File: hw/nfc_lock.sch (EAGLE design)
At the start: 27 parts, among them IC1 STM8S003F3, IC3 MCP170312MB, Q1 8MHz, U1 M24SR16-YMN6T/2, U2 IRFML8244TRPBF, U3 IRFML8244TRPBF, U4 2N7002BKW, X1 MINI-USB-32005-301

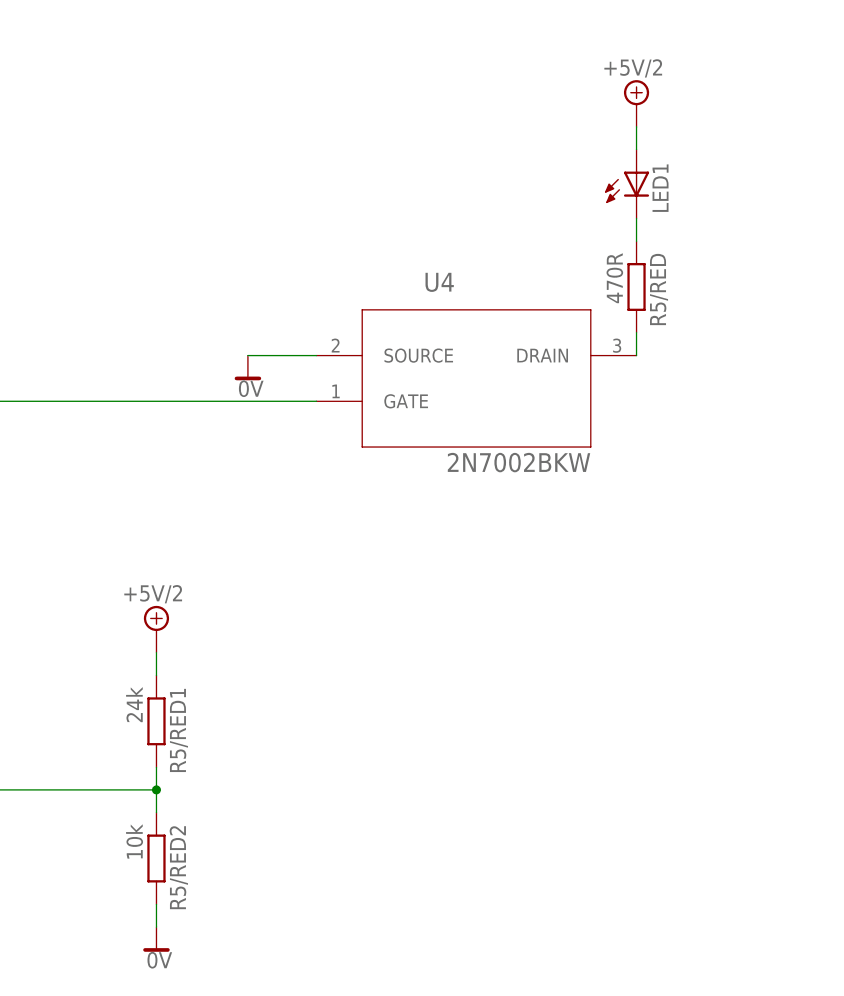
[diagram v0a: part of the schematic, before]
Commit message: resistors not LEDs for voltage split
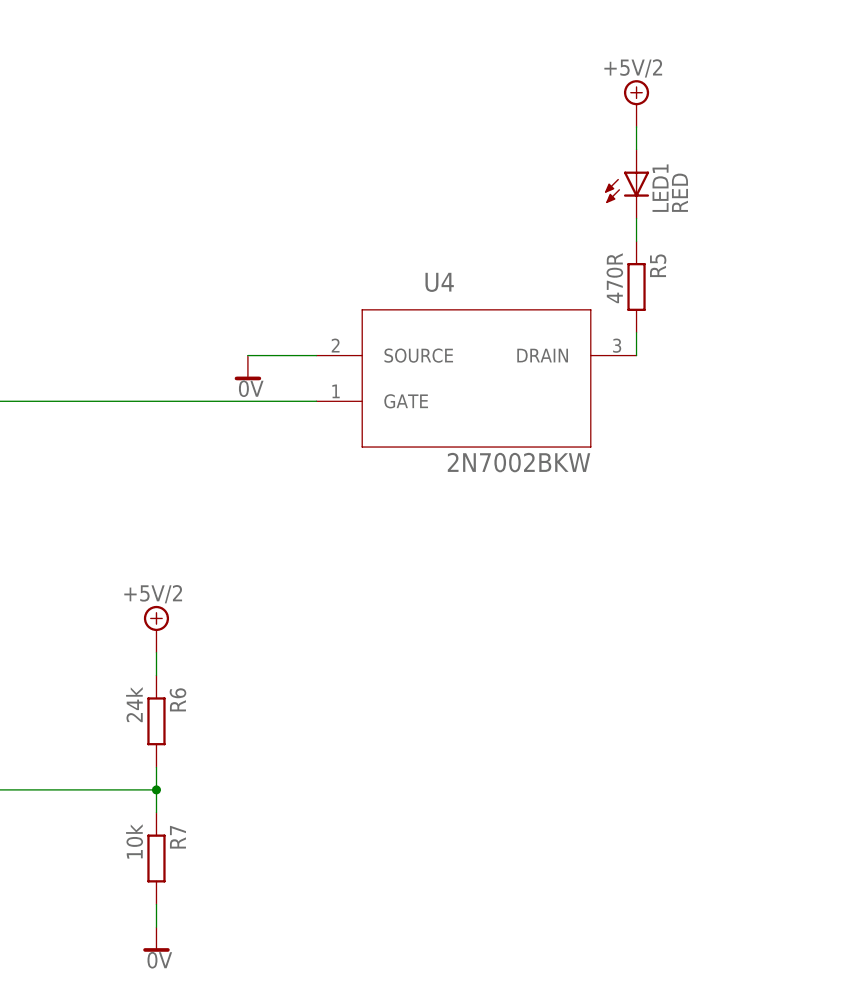
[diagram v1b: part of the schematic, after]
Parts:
- LED1: value (none) -> RED
- renumbered R5/RED to R5, R5/RED1 to R6, R5/RED2 to R7
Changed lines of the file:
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@@
 <part name="SUPPLY25" library="supply2" deviceset="+5V/1" device="" value="+3.3V"/>
 <part name="U4" library="2n7002" deviceset="2N7002BKW" device=""/>
-<part name="LED1" library="led" deviceset="LED" device="CHIP-LED0603"/>
-<part name="R5/RED" library="rcl" deviceset="R-EU_" device="R0805" value="470R"/>
+<part name="LED1" library="led" deviceset="LED" device="CHIP-LED0603" value="RED"/>
+<part name="R5" library="rcl" deviceset="R-EU_" device="R0805" value="470R"/>
 <part name="SUPPLY26" library="supply2" deviceset="0V" device=""/>
 <part name="C4" library="rcl" deviceset="CPOL-EU" device="153CLV-0405" value="1uF"/>
@@
 <part name="SUPPLY28" library="supply2" deviceset="0V" device=""/>
 <part name="SUPPLY29" library="supply2" deviceset="0V" device=""/>
-<part name="R5/RED1" library="rcl" deviceset="R-EU_" device="R0805" value="24k"/>
-<part name="R5/RED2" library="rcl" deviceset="R-EU_" device="R0805" value="10k"/>
+<part name="R6" library="rcl" deviceset="R-EU_" device="R0805" value="24k"/>
+<part name="R7" library="rcl" deviceset="R-EU_" device="R0805" value="10k"/>
 <part name="SUPPLY30" library="supply2" deviceset="0V" device=""/>
 <part name="SUPPLY31" library="supply2" deviceset="+5V/2" device=""/>
@@
 <instance part="U4" gate="A" x="116.84" y="0"/>
 <instance part="LED1" gate="G$1" x="152.4" y="20.32"/>
-<instance part="R5/RED" gate="G$1" x="152.4" y="7.62" rot="R270"/>
+<instance part="R5" gate="G$1" x="152.4" y="7.62" rot="R270"/>
 <instance part="SUPPLY26" gate="0V" x="109.22" y="-2.54"/>
 <instance part="C4" gate="G$1" x="-15.24" y="81.28"/>
@@
 <instance part="SUPPLY28" gate="0V" x="-33.02" y="60.96"/>
 <instance part="SUPPLY29" gate="0V" x="-33.02" y="53.34"/>
-<instance part="R5/RED1" gate="G$1" x="99.06" y="-40.64" rot="R270"/>
-<instance part="R5/RED2" gate="G$1" x="99.06" y="-55.88" rot="R270"/>
+<instance part="R6" gate="G$1" x="99.06" y="-40.64" rot="R270"/>
+<instance part="R7" gate="G$1" x="99.06" y="-55.88" rot="R270"/>
 <instance part="SUPPLY30" gate="0V" x="99.06" y="-66.04"/>
 <instance part="SUPPLY31" gate="G$1" x="-63.5" y="111.76"/>
@@
 </segment>
 <segment>
-<pinref part="R5/RED2" gate="G$1" pin="2"/>
+<pinref part="R7" gate="G$1" pin="2"/>
 <pinref part="SUPPLY30" gate="0V" pin="0V"/>
 <wire x1="99.06" y1="-63.5" x2="99.06" y2="-60.96" width="0.1524" layer="91"/>
@@
 </segment>
 <segment>
-<pinref part="R5/RED1" gate="G$1" pin="1"/>
+<pinref part="R6" gate="G$1" pin="1"/>
 <pinref part="SUPPLY32" gate="G$1" pin="+5V/2"/>
 <wire x1="99.06" y1="-33.02" x2="99.06" y2="-35.56" width="0.1524" layer="91"/>
@@
 <segment>
 <pinref part="LED1" gate="G$1" pin="C"/>
-<pinref part="R5/RED" gate="G$1" pin="1"/>
+<pinref part="R5" gate="G$1" pin="1"/>
 <wire x1="152.4" y1="15.24" x2="152.4" y2="12.7" width="0.1524" layer="91"/>
 </segment>
@@
 <net name="N$14" class="0">
 <segment>
-<pinref part="R5/RED" gate="G$1" pin="2"/>
+<pinref part="R5" gate="G$1" pin="2"/>
 <pinref part="U4" gate="A" pin="DRAIN"/>
 <wire x1="152.4" y1="0" x2="152.4" y2="2.54" width="0.1524" layer="91"/>
@@
 <wire x1="63.5" y1="66.04" x2="63.5" y2="-48.26" width="0.1524" layer="91"/>
 <wire x1="63.5" y1="-48.26" x2="99.06" y2="-48.26" width="0.1524" layer="91"/>
-<pinref part="R5/RED1" gate="G$1" pin="2"/>
-<pinref part="R5/RED2" gate="G$1" pin="1"/>
+<pinref part="R6" gate="G$1" pin="2"/>
+<pinref part="R7" gate="G$1" pin="1"/>
 <wire x1="99.06" y1="-50.8" x2="99.06" y2="-48.26" width="0.1524" layer="91"/>
 <wire x1="99.06" y1="-48.26" x2="99.06" y2="-45.72" width="0.1524" layer="91"/>

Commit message: antenna drawed
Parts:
- added R8: 30k, rcl:R-EU_R0805
- R4: value 10k -> 20k
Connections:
- net +5V/1: now also R8.2
- net N$7: now also R8.1
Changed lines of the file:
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@@
 <part name="SUPPLY23" library="supply2" deviceset="0V" device=""/>
 <part name="SUPPLY24" library="supply2" deviceset="0V" device=""/>
-<part name="R4" library="rcl" deviceset="R-EU_" device="R0805" value="10k"/>
+<part name="R4" library="rcl" deviceset="R-EU_" device="R0805" value="20k"/>
 <part name="SUPPLY25" library="supply2" deviceset="+5V/1" device="" value="+3.3V"/>
 <part name="U4" library="2n7002" deviceset="2N7002BKW" device=""/>
@@
 <part name="SUPPLY22" library="supply2" deviceset="+5V/2" device=""/>
 <part name="SUPPLY32" library="supply2" deviceset="+5V/2" device=""/>
+<part name="R8" library="rcl" deviceset="R-EU_" device="R0805" value="30k"/>
+<part name="SUPPLY33" library="supply2" deviceset="+5V/1" device="" value="+3.3V"/>
 </parts>
 <sheets>
@@
 <instance part="SUPPLY22" gate="G$1" x="152.4" y="27.94"/>
 <instance part="SUPPLY32" gate="G$1" x="99.06" y="-30.48"/>
+<instance part="R8" gate="G$1" x="96.52" y="99.06" rot="R90"/>
+<instance part="SUPPLY33" gate="G$1" x="96.52" y="109.22"/>
 </instances>
 <busses>
@@
 <pinref part="SUPPLY25" gate="G$1" pin="+5V/1"/>
 <wire x1="167.64" y1="99.06" x2="167.64" y2="96.52" width="0.1524" layer="91"/>
+</segment>
+<segment>
+<pinref part="R8" gate="G$1" pin="2"/>
+<pinref part="SUPPLY33" gate="G$1" pin="+5V/1"/>
+<wire x1="96.52" y1="106.68" x2="96.52" y2="104.14" width="0.1524" layer="91"/>
 </segment>
 </net>
@@
 <pinref part="U1" gate="G$1" pin="RFDISABLE"/>
 <wire x1="96.52" y1="81.28" x2="111.76" y2="81.28" width="0.1524" layer="91"/>
-</segment>
-</net>
+<pinref part="R8" gate="G$1" pin="1"/>
+<junction x="96.52" y="93.98"/>
+</segment>
+</net>

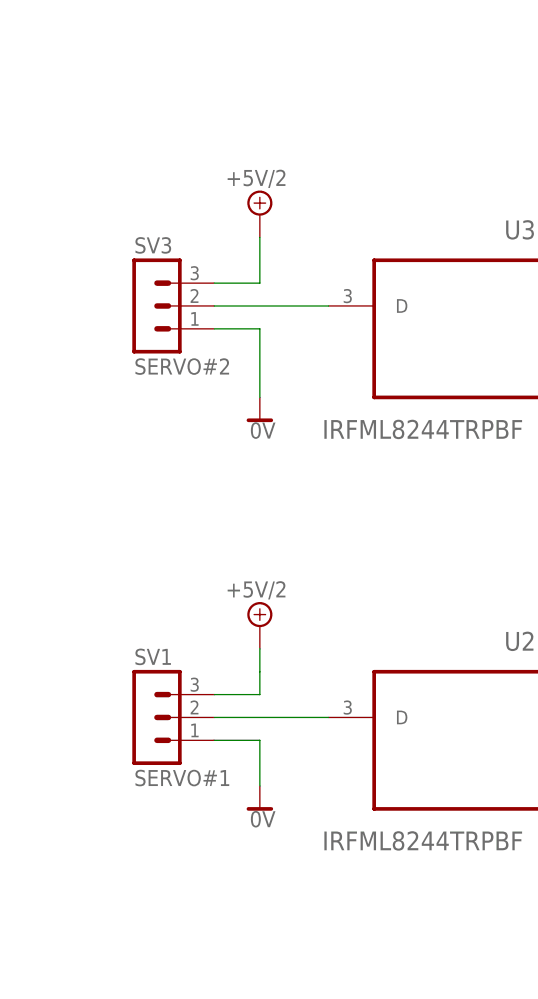
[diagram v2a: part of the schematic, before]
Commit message: added 2x more servos + some elements positioning
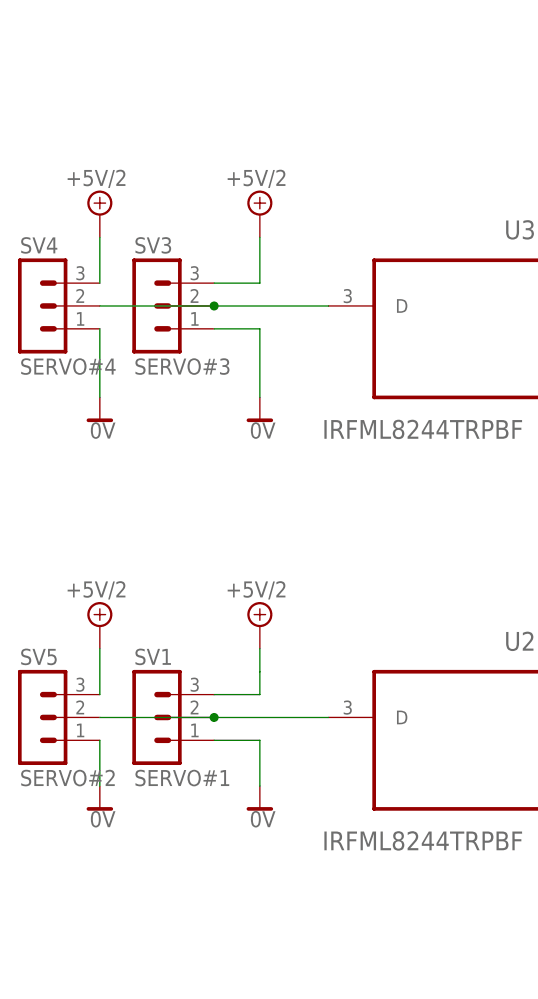
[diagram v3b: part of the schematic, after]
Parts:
- added SV4: SERVO#4, con-lstb:MA03-1
- added SV5: SERVO#2, con-lstb:MA03-1
- SV3: value SERVO#2 -> SERVO#3
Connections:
- net +5V/2: now also SV4.3, SV5.3
- net 0V: now also SV4.1, SV5.1
- net N$11: now also SV4.2
- net N$9: now also SV5.2
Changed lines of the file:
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@@
 <part name="SV2" library="con-lstb" deviceset="MA04-1" device="" value="SWIM"/>
 <part name="SUPPLY21" library="supply2" deviceset="0V" device=""/>
-<part name="SV3" library="con-lstb" deviceset="MA03-1" device="" value="SERVO#2"/>
+<part name="SV3" library="con-lstb" deviceset="MA03-1" device="" value="SERVO#3"/>
 <part name="SUPPLY23" library="supply2" deviceset="0V" device=""/>
 <part name="SUPPLY24" library="supply2" deviceset="0V" device=""/>
@@
 <part name="R8" library="rcl" deviceset="R-EU_" device="R0805" value="30k"/>
 <part name="SUPPLY33" library="supply2" deviceset="+5V/1" device="" value="+3.3V"/>
+<part name="SV4" library="con-lstb" deviceset="MA03-1" device="" value="SERVO#4"/>
+<part name="SV5" library="con-lstb" deviceset="MA03-1" device="" value="SERVO#2"/>
+<part name="SUPPLY34" library="supply2" deviceset="0V" device=""/>
+<part name="SUPPLY35" library="supply2" deviceset="+5V/2" device=""/>
+<part name="SUPPLY36" library="supply2" deviceset="+5V/2" device=""/>
+<part name="SUPPLY37" library="supply2" deviceset="0V" device=""/>
 </parts>
 <sheets>
@@
 <instance part="R8" gate="G$1" x="96.52" y="99.06" rot="R90"/>
 <instance part="SUPPLY33" gate="G$1" x="96.52" y="109.22"/>
+<instance part="SV4" gate="G$1" x="-137.16" y="20.32"/>
+<instance part="SV5" gate="G$1" x="-137.16" y="-25.4"/>
+<instance part="SUPPLY34" gate="0V" x="-129.54" y="7.62"/>
+<instance part="SUPPLY35" gate="G$1" x="-129.54" y="30.48"/>
+<instance part="SUPPLY36" gate="G$1" x="-129.54" y="-15.24"/>
+<instance part="SUPPLY37" gate="0V" x="-129.54" y="-35.56"/>
 </instances>
 <busses>
@@
 <pinref part="SUPPLY30" gate="0V" pin="0V"/>
 <wire x1="99.06" y1="-63.5" x2="99.06" y2="-60.96" width="0.1524" layer="91"/>
+</segment>
+<segment>
+<pinref part="SV4" gate="G$1" pin="1"/>
+<pinref part="SUPPLY34" gate="0V" pin="0V"/>
+<wire x1="-129.54" y1="10.16" x2="-129.54" y2="17.78" width="0.1524" layer="91"/>
+</segment>
+<segment>
+<pinref part="SV5" gate="G$1" pin="1"/>
+<pinref part="SUPPLY37" gate="0V" pin="0V"/>
+<wire x1="-129.54" y1="-33.02" x2="-129.54" y2="-27.94" width="0.1524" layer="91"/>
 </segment>
 </net>
@@
 <wire x1="99.06" y1="-33.02" x2="99.06" y2="-35.56" width="0.1524" layer="91"/>
 </segment>
+<segment>
+<pinref part="SV4" gate="G$1" pin="3"/>
+<pinref part="SUPPLY35" gate="G$1" pin="+5V/2"/>
+<wire x1="-129.54" y1="27.94" x2="-129.54" y2="22.86" width="0.1524" layer="91"/>
+</segment>
+<segment>
+<pinref part="SV5" gate="G$1" pin="3"/>
+<pinref part="SUPPLY36" gate="G$1" pin="+5V/2"/>
+<wire x1="-129.54" y1="-17.78" x2="-129.54" y2="-22.86" width="0.1524" layer="91"/>
+</segment>
 </net>
 <net name="N$3" class="0">
@@
 <pinref part="SV1" gate="G$1" pin="2"/>
 <wire x1="-116.84" y1="-25.4" x2="-104.14" y2="-25.4" width="0.1524" layer="91"/>
+<pinref part="SV5" gate="G$1" pin="2"/>
+<wire x1="-129.54" y1="-25.4" x2="-116.84" y2="-25.4" width="0.1524" layer="91"/>
+<junction x="-116.84" y="-25.4"/>
 </segment>
 </net>
@@
 <pinref part="SV3" gate="G$1" pin="2"/>
 <wire x1="-116.84" y1="20.32" x2="-104.14" y2="20.32" width="0.1524" layer="91"/>
-</segment>
-</net>
+<pinref part="SV4" gate="G$1" pin="2"/>
+<wire x1="-129.54" y1="20.32" x2="-116.84" y2="20.32" width="0.1524" layer="91"/>
+<junction x="-116.84" y="20.32"/>
+</segment>
+</net>

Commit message: fixed packaging of 2n7002 transistor
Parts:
- removed U4: 2N7002BKW, 2n7002:2N7002BKW
- added Q3: 2N7002,215, Common-Parts-Library-Eagle:2N7002,215
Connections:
- net 0V: now also Q3.S; no longer U4.SOURCE
- net N$14: now also Q3.D; no longer U4.DRAIN
- net N$19: now also Q3.G; no longer U4.GATE
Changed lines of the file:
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@@
 <part name="R4" library="rcl" deviceset="R-EU_" device="R0805" value="20k"/>
 <part name="SUPPLY25" library="supply2" deviceset="+5V/1" device="" value="+3.3V"/>
-<part name="U4" library="2n7002" deviceset="2N7002BKW" device=""/>
 <part name="LED1" library="led" deviceset="LED" device="CHIP-LED0603" value="RED"/>
 <part name="R5" library="rcl" deviceset="R-EU_" device="R0805" value="470R"/>
@@
 <part name="SUPPLY36" library="supply2" deviceset="+5V/2" device=""/>
 <part name="SUPPLY37" library="supply2" deviceset="0V" device=""/>
+<part name="Q3" library="Common-Parts-Library-Eagle" deviceset="2N7002,215" device=""/>
 </parts>
 <sheets>
@@
 <instance part="R4" gate="G$1" x="167.64" y="91.44" rot="R90"/>
 <instance part="SUPPLY25" gate="G$1" x="167.64" y="101.6"/>
-<instance part="U4" gate="A" x="116.84" y="0"/>
 <instance part="LED1" gate="G$1" x="152.4" y="20.32"/>
 <instance part="R5" gate="G$1" x="152.4" y="7.62" rot="R270"/>
-<instance part="SUPPLY26" gate="0V" x="109.22" y="-2.54"/>
+<instance part="SUPPLY26" gate="0V" x="152.4" y="-20.32"/>
 <instance part="C4" gate="G$1" x="-15.24" y="81.28"/>
 <instance part="SUPPLY27" gate="0V" x="-15.24" y="68.58"/>
@@
 <instance part="SUPPLY36" gate="G$1" x="-129.54" y="-15.24"/>
 <instance part="SUPPLY37" gate="0V" x="-129.54" y="-35.56"/>
+<instance part="Q3" gate="G$1" x="149.86" y="-7.62"/>
 </instances>
 <busses>
@@
 </segment>
 <segment>
-<pinref part="U4" gate="A" pin="SOURCE"/>
-<pinref part="SUPPLY26" gate="0V" pin="0V"/>
-<wire x1="109.22" y1="0" x2="116.84" y2="0" width="0.1524" layer="91"/>
-</segment>
-<segment>
 <pinref part="C4" gate="G$1" pin="-"/>
 <pinref part="SUPPLY27" gate="0V" pin="0V"/>
@@
 <pinref part="SUPPLY37" gate="0V" pin="0V"/>
 <wire x1="-129.54" y1="-33.02" x2="-129.54" y2="-27.94" width="0.1524" layer="91"/>
+</segment>
+<segment>
+<pinref part="Q3" gate="G$1" pin="S"/>
+<pinref part="SUPPLY26" gate="0V" pin="0V"/>
+<wire x1="152.4" y1="-17.78" x2="152.4" y2="-15.24" width="0.1524" layer="91"/>
 </segment>
 </net>
@@
 <segment>
 <pinref part="R5" gate="G$1" pin="2"/>
-<pinref part="U4" gate="A" pin="DRAIN"/>
 <wire x1="152.4" y1="0" x2="152.4" y2="2.54" width="0.1524" layer="91"/>
+<pinref part="Q3" gate="G$1" pin="D"/>
 </segment>
 </net>
@@
 <pinref part="IC1" gate="G$1" pin="PC6/SPI_MOSI/[TIM1_CH1]"/>
 <wire x1="58.42" y1="76.2" x2="68.58" y2="76.2" width="0.1524" layer="91"/>
-<wire x1="68.58" y1="76.2" x2="68.58" y2="-5.08" width="0.1524" layer="91"/>
-<pinref part="U4" gate="A" pin="GATE"/>
-<wire x1="68.58" y1="-5.08" x2="116.84" y2="-5.08" width="0.1524" layer="91"/>
-</segment>
-</net>
+<wire x1="68.58" y1="76.2" x2="68.58" y2="-10.16" width="0.1524" layer="91"/>
+<wire x1="68.58" y1="-10.16" x2="144.78" y2="-10.16" width="0.1524" layer="91"/>
+<pinref part="Q3" gate="G$1" pin="G"/>
+</segment>
+</net>

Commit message: adjusted sizes of different components to match what i have in a closet... ;)
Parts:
- removed C6: 33pF, rcl:C-EUC1206
- added C8: 33pF, rcl:C-EUC0402
- C1: device rcl:C-EUC1206 -> rcl:C-EUC0603K
- C5: device rcl:C-EUC1206 -> rcl:C-EUC0402
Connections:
- net 0V: now also C8.1; no longer C6.2
- net N$16: now also C8.2; no longer C5.2
- net N$17: now also C5.2; no longer C6.1
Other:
- moved on the sheet: C5
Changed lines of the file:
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@@
 <part name="SUPPLY11" library="supply2" deviceset="+5V/1" device="" value="+3.3V"/>
 <part name="R1" library="rcl" deviceset="R-EU_" device="R0805" value="10k"/>
-<part name="C1" library="rcl" deviceset="C-EU" device="C1206" value="10nF"/>
+<part name="C1" library="rcl" deviceset="C-EU" device="C0603K" value="10nF"/>
 <part name="SUPPLY12" library="supply2" deviceset="+5V/1" device="" value="+3.3V"/>
 <part name="SUPPLY13" library="supply2" deviceset="0V" device=""/>
@@
 <part name="SUPPLY27" library="supply2" deviceset="0V" device=""/>
 <part name="Q1" library="crystal" deviceset="CRYSTAL" device="SM49" value="8MHz"/>
-<part name="C5" library="rcl" deviceset="C-EU" device="C1206" value="33pF"/>
-<part name="C6" library="rcl" deviceset="C-EU" device="C1206" value="33pF"/>
 <part name="SUPPLY28" library="supply2" deviceset="0V" device=""/>
 <part name="SUPPLY29" library="supply2" deviceset="0V" device=""/>
@@
 <part name="SUPPLY37" library="supply2" deviceset="0V" device=""/>
 <part name="Q3" library="Common-Parts-Library-Eagle" deviceset="2N7002,215" device=""/>
+<part name="C8" library="rcl" deviceset="C-EU" device="C0402" value="33pF"/>
+<part name="C5" library="rcl" deviceset="C-EU" device="C0402" value="33pF"/>
 </parts>
 <sheets>
@@
 <instance part="SUPPLY27" gate="0V" x="-15.24" y="68.58"/>
 <instance part="Q1" gate="G$1" x="-22.86" y="60.96" rot="R90"/>
-<instance part="C5" gate="G$1" x="-27.94" y="63.5" rot="R90"/>
-<instance part="C6" gate="G$1" x="-25.4" y="55.88" rot="R270"/>
 <instance part="SUPPLY28" gate="0V" x="-33.02" y="60.96"/>
 <instance part="SUPPLY29" gate="0V" x="-33.02" y="53.34"/>
@@
 <instance part="SUPPLY37" gate="0V" x="-129.54" y="-35.56"/>
 <instance part="Q3" gate="G$1" x="149.86" y="-7.62"/>
+<instance part="C8" gate="G$1" x="-27.94" y="63.5" rot="R90"/>
+<instance part="C5" gate="G$1" x="-27.94" y="55.88" rot="R90"/>
 </instances>
 <busses>
@@
 </segment>
 <segment>
-<pinref part="C5" gate="G$1" pin="1"/>
 <pinref part="SUPPLY28" gate="0V" pin="0V"/>
 <wire x1="-33.02" y1="63.5" x2="-30.48" y2="63.5" width="0.1524" layer="91"/>
-</segment>
-<segment>
-<pinref part="C6" gate="G$1" pin="2"/>
+<pinref part="C8" gate="G$1" pin="1"/>
+</segment>
+<segment>
 <pinref part="SUPPLY29" gate="0V" pin="0V"/>
 <wire x1="-33.02" y1="55.88" x2="-30.48" y2="55.88" width="0.1524" layer="91"/>
+<pinref part="C5" gate="G$1" pin="1"/>
 </segment>
 <segment>
@@
 <pinref part="Q1" gate="G$1" pin="2"/>
 <wire x1="-22.86" y1="63.5" x2="-10.16" y2="63.5" width="0.1524" layer="91"/>
-<pinref part="C5" gate="G$1" pin="2"/>
+<pinref part="C8" gate="G$1" pin="2"/>
 <junction x="-22.86" y="63.5"/>
 </segment>
@@
 <wire x1="-22.86" y1="58.42" x2="-22.86" y2="55.88" width="0.1524" layer="91"/>
 <wire x1="-22.86" y1="55.88" x2="-10.16" y2="55.88" width="0.1524" layer="91"/>
-<pinref part="C6" gate="G$1" pin="1"/>
+<pinref part="C5" gate="G$1" pin="2"/>
 <junction x="-22.86" y="55.88"/>
 </segment>
